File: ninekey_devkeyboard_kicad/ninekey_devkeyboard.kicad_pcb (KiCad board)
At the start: 2 copper layers, 90 x 90 mm, 19 parts, among them SW1 SW_Push_Dual_x2, SW2 SW_Push_Dual_x2, SW3 SW_Push_Dual_x2, SW4 SW_Push_Dual_x2, SW5 SW_Push_Dual_x2, SW6 SW_Push_Dual_x2, SW7 SW_Push_Dual_x2, SW8 SW_Push_Dual_x2, SW9 SW_Push_Dual_x2

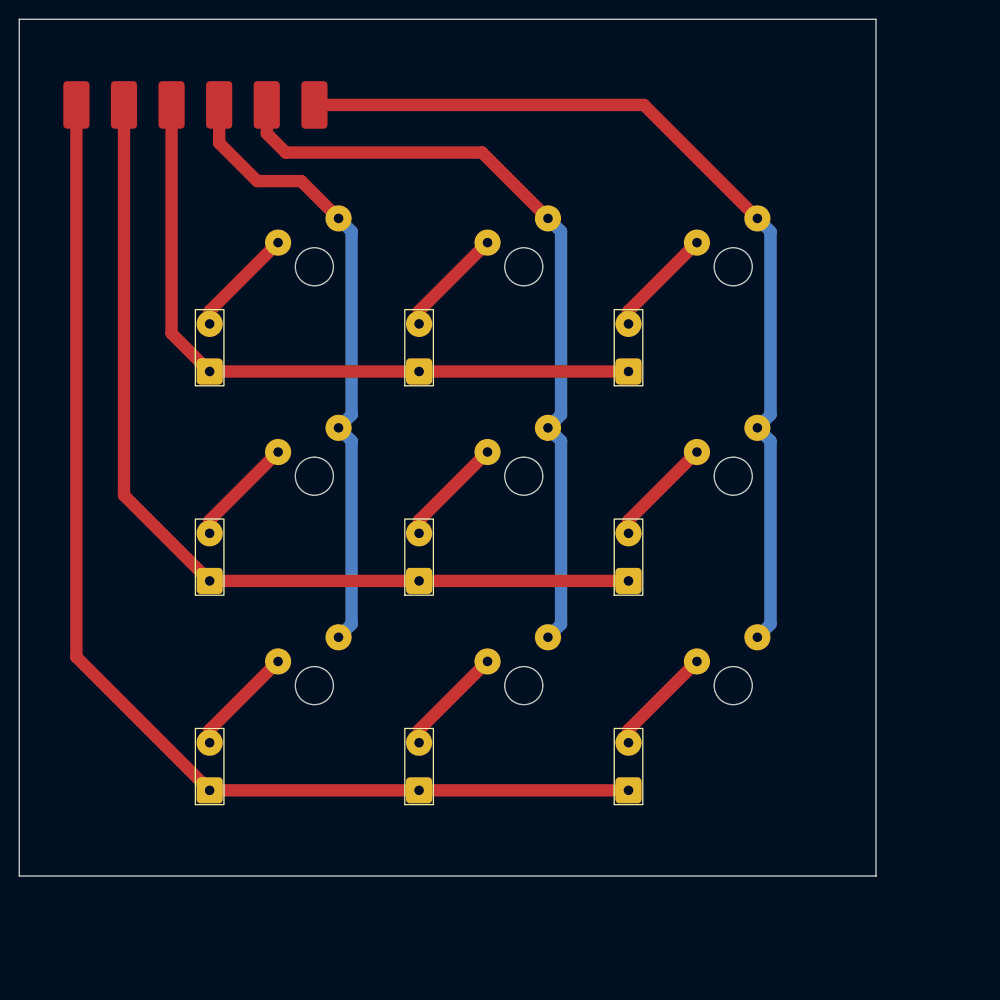
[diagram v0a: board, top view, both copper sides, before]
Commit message: Сделал новую разводку
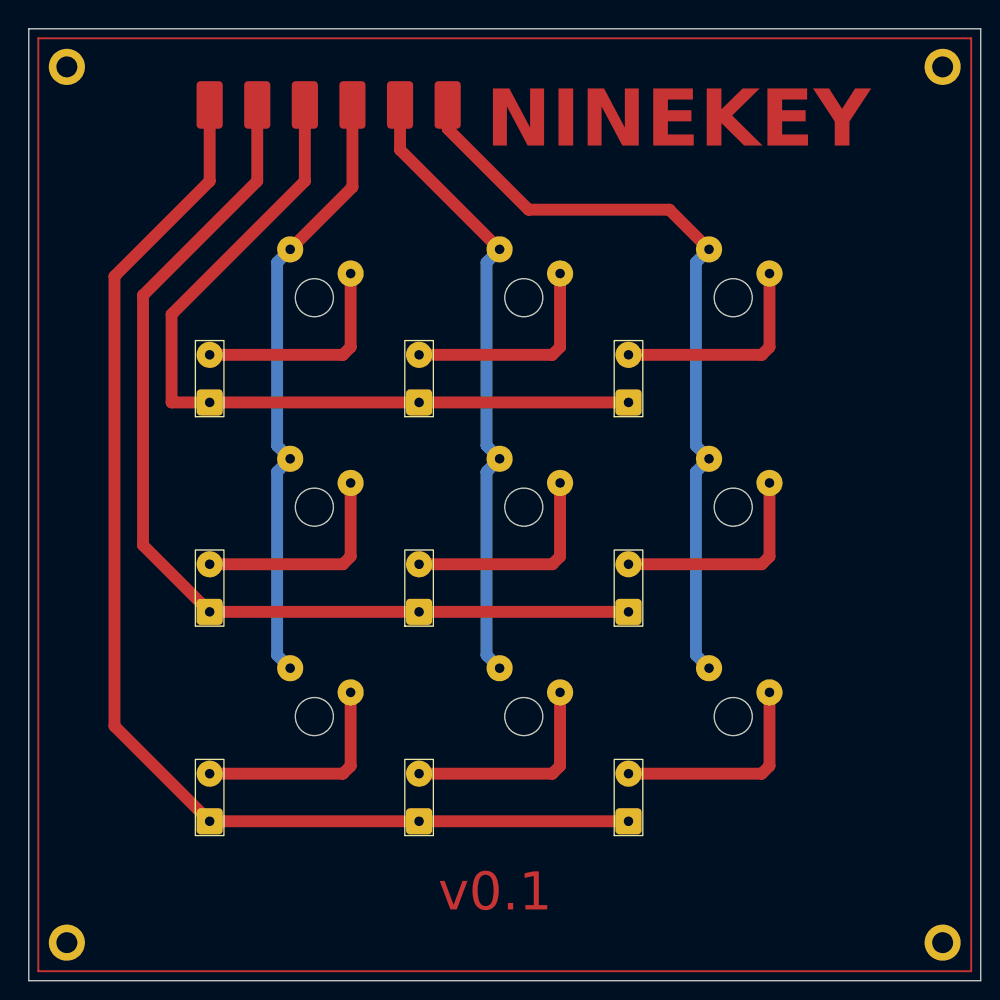
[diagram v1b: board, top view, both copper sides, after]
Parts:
- added ?: , , F.Cu at (200.0, 52.0)
- added ?: , , F.Cu at (108.0, 52.0)
- added ?: , , F.Cu at (200.0, 144.0)
- added REF**: MountingHole_2.2mm_M2_DIN965_Pad, MountingHole:MountingHole_2.2mm_M2_DIN965_Pad, F.Cu at (108.0, 144.0)
- SW1, SW2, SW3, SW4, SW5, SW6, SW7, SW8, SW9: moved to B.Cu
- moved CONNECTOR1 14.0 mm to (273.0, 46.0)
- moved SW1 6.03 mm to (131.5, 71.2), turned to 180 degrees
- moved SW2 6.03 mm to (153.5, 71.2), turned to 180 degrees
- moved SW3 6.03 mm to (175.5, 71.2), turned to 180 degrees
- moved SW4 6.03 mm to (131.5, 93.2), turned to 180 degrees
- moved SW5 6.03 mm to (153.5, 93.2), turned to 180 degrees
- moved SW6 6.03 mm to (175.5, 93.2), turned to 180 degrees
- moved SW7 6.03 mm to (131.5, 115.2), turned to 180 degrees
- moved SW8 6.03 mm to (153.5, 115.2), turned to 180 degrees
- moved SW9 6.03 mm to (175.5, 115.2), turned to 180 degrees
- moved D1 3.25 mm to (123.0, 84.8)
- moved D2 3.25 mm to (145.0, 84.8)
- moved D3 3.25 mm to (167.0, 84.8)
- moved D4 3.25 mm to (123.0, 106.8)
- moved D5 3.25 mm to (145.0, 106.8)
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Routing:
- net Net-(CONNECTOR1-COL_1): track 82.5 -> 65.8 mm
- net Net-(CONNECTOR1-COL_2): track 97.8 -> 81.5 mm
- net Net-(CONNECTOR1-ROW_0): track 73.7 -> 85.0 mm
- net Net-(D9-A): track 11.5 -> 22.9 mm
- net Net-(D8-A): track 11.5 -> 22.9 mm
- net Net-(D7-A): track 11.5 -> 22.9 mm
- net Net-(D6-A): track 11.5 -> 22.9 mm
- net Net-(D5-A): track 11.5 -> 22.9 mm
- net Net-(D4-A): track 11.5 -> 22.9 mm
- net Net-(D3-A): track 11.5 -> 22.9 mm
- net Net-(D2-A): track 11.5 -> 22.9 mm
- net Net-(D1-A): track 11.5 -> 22.9 mm
- net Net-(CONNECTOR1-ROW_1): track 97.7 -> 105.1 mm
- net Net-(CONNECTOR1-ROW_2): track 121.8 -> 127.5 mm
- net Net-(CONNECTOR1-COL_0): track 66.1 -> 64.2 mm
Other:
- board size 90 x 90 mm -> 100 x 100 mm
- board text added: "NINEKEY"
- board text added: "v0.1"

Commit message: Переставил диоды
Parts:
- moved SW2 88.5 mm to (69.5, 43.2)
- moved SW3 88.5 mm to (91.5, 43.2)
- moved SW5 88.5 mm to (69.5, 65.2)
- moved SW6 88.5 mm to (91.5, 65.2)
- moved SW8 88.5 mm to (69.5, 87.2)
- moved SW9 88.5 mm to (91.5, 87.2)
- moved ? 88.5 mm to (116.0, 24.0)
- moved ? 88.5 mm to (24.0, 24.0)
- moved ? 88.5 mm to (116.0, 116.0)
- moved CONNECTOR1 88.5 mm to (189.0, 18.0)
- moved REF** 88.5 mm to (24.0, 116.0)
- moved SW1 88.5 mm to (47.5, 43.2)
- moved SW4 88.5 mm to (47.5, 65.2)
- moved SW7 88.5 mm to (47.5, 87.2)
- moved D1 68.0 mm to (61.0, 56.8)
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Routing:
- net Net-(CONNECTOR1-ROW_2): track 127.5 -> 148.2 mm
- net Net-(CONNECTOR1-ROW_1): track 105.1 -> 122.6 mm
- net Net-(CONNECTOR1-ROW_0): track 85.0 -> 97.0 mm
- net Net-(D3-A): track 22.9 -> 11.5 mm
- net Net-(D2-A): track 22.9 -> 11.5 mm
- net Net-(D1-A): track 22.9 -> 11.5 mm
- net Net-(D9-A): track 22.9 -> 11.5 mm
- net Net-(D8-A): track 22.9 -> 11.5 mm
- net Net-(D7-A): track 22.9 -> 11.5 mm
- net Net-(D6-A): track 22.9 -> 11.5 mm
- net Net-(D5-A): track 22.9 -> 11.5 mm
- net Net-(D4-A): track 22.9 -> 11.5 mm
